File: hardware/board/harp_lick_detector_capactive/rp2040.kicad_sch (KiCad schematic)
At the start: 46 parts

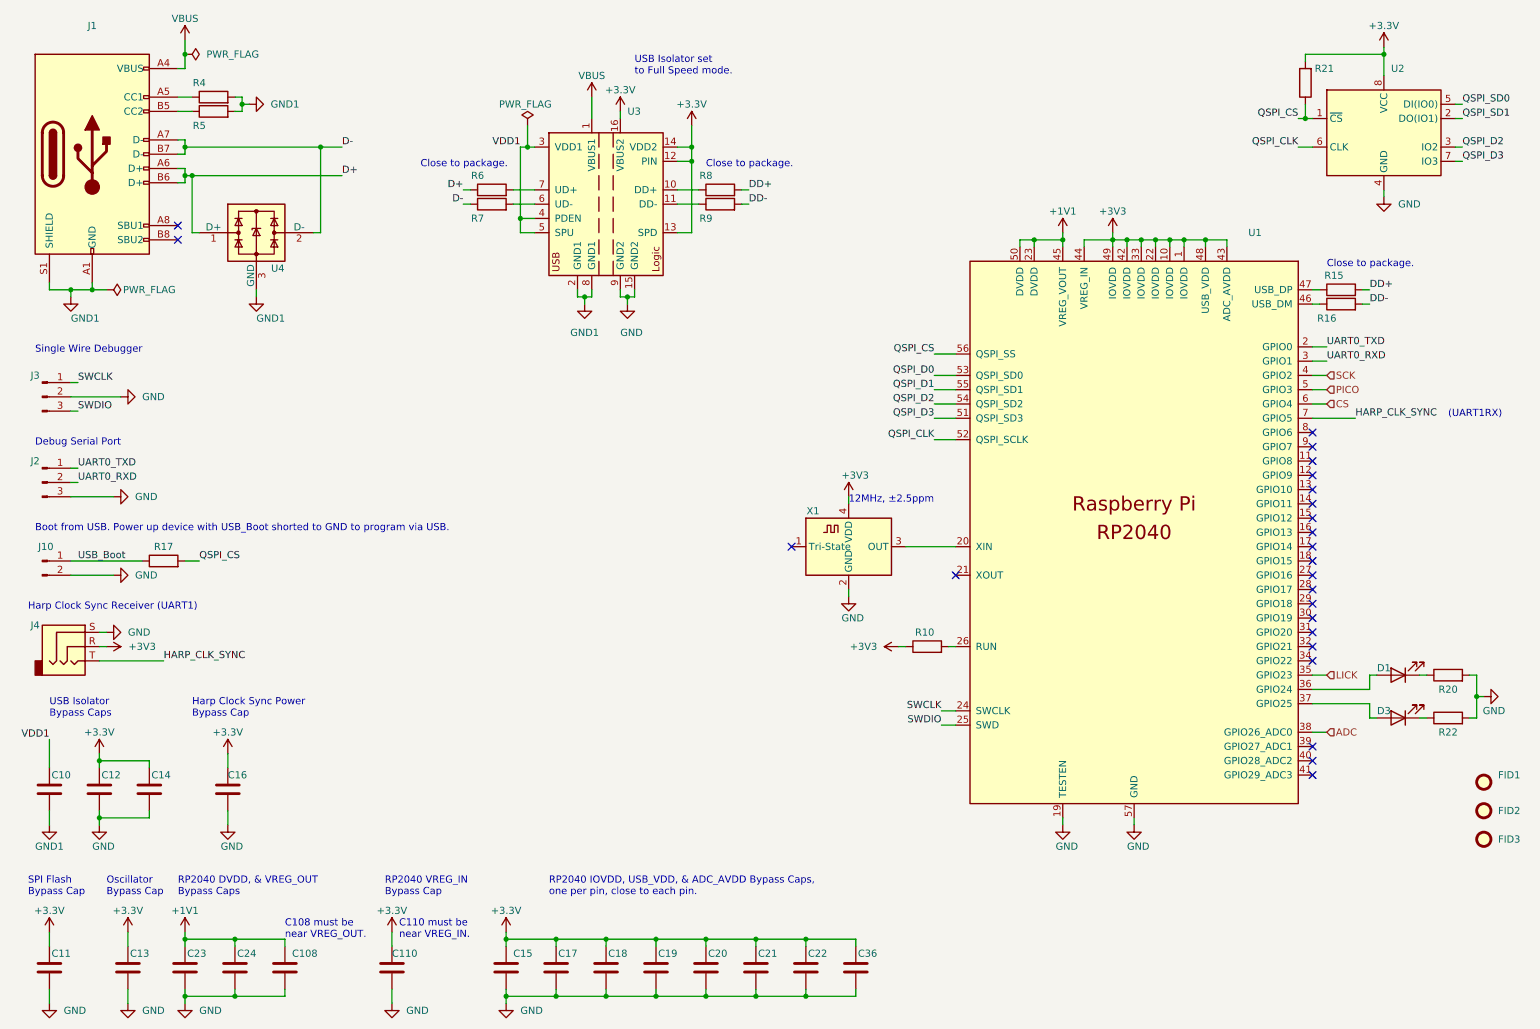
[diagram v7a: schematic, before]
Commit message: change usb connector; more layout
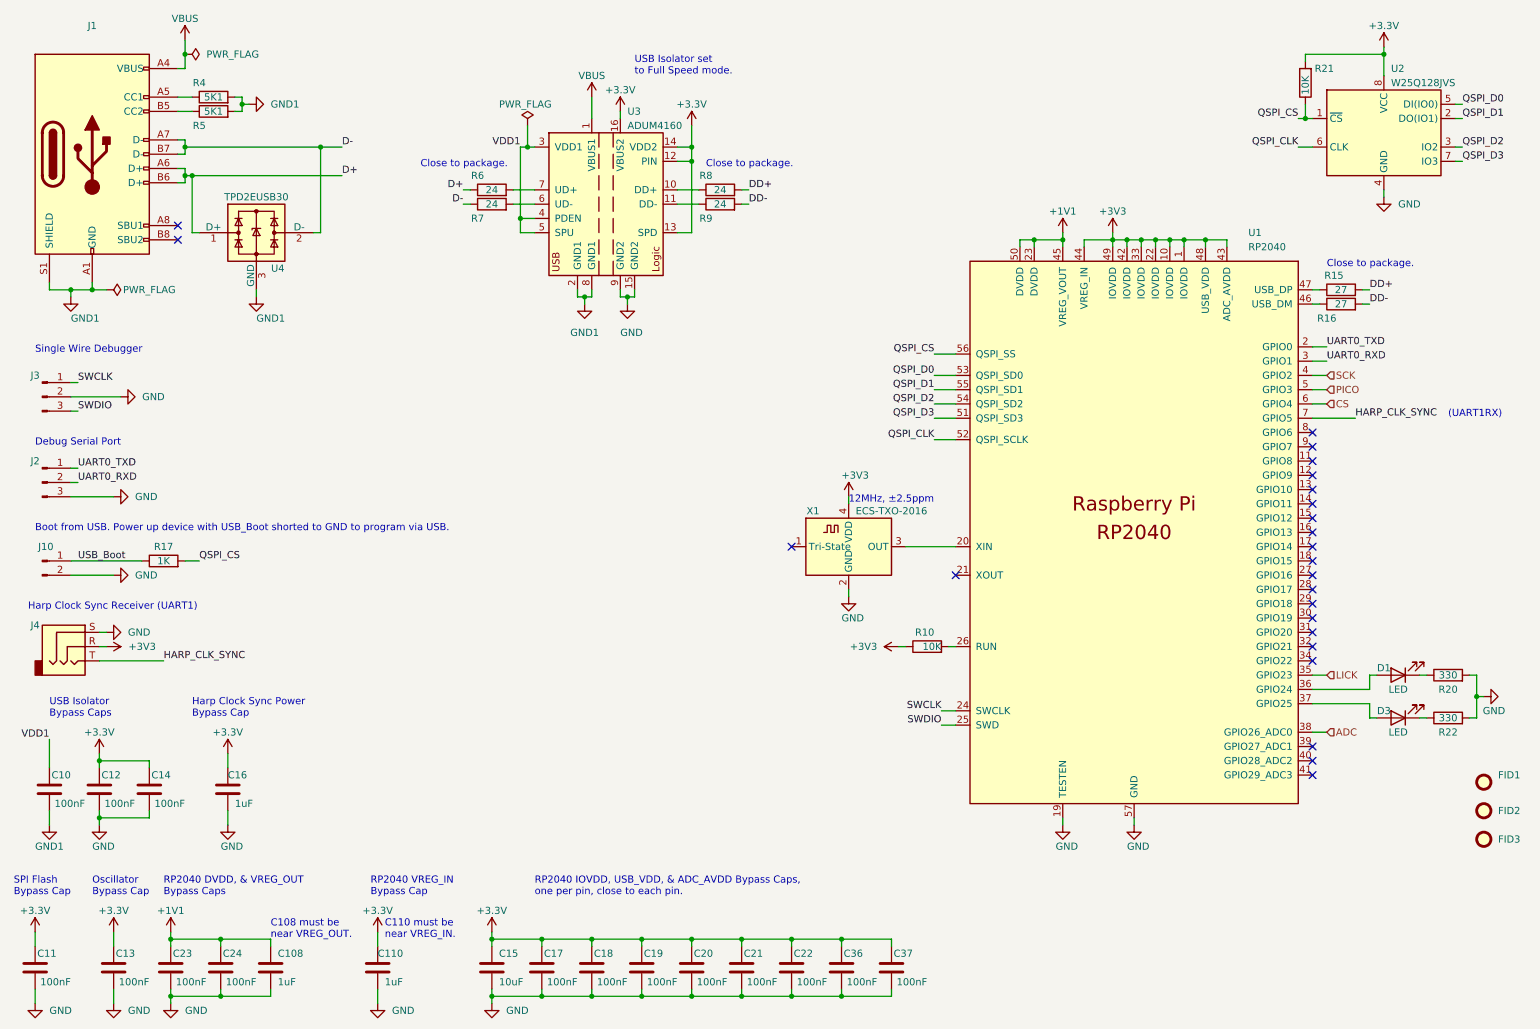
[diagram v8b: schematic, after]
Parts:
- added C37: 100nF, Capacitor_SMD:C_0402_1005Metric_Pad0.74x0.62mm_HandSolder, symbol Device:C
- C10, C11, C12, C13, C14, C17, C18, C19, C20, C21, C22, C23, C24, C36: value (none) -> 100nF; footprint (none) -> Capacitor_SMD:C_0402_1005Metric_Pad0.74x0.62mm_HandSolder
- C108, C110, C16: value (none) -> 1uF; footprint (none) -> Capacitor_SMD:C_0603_1608Metric_Pad1.08x0.95mm_HandSolder
- C15: value (none) -> 10uF; footprint (none) -> Capacitor_SMD:C_0805_2012Metric
- D1, D3: value (none) -> LED; footprint (none) -> LED_SMD:LED_0603_1608Metric_Pad1.05x0.95mm_HandSolder
- FID1, FID2, FID3: value (none) -> Fiducial; footprint (none) -> Fiducial:Fiducial_0.5mm_Mask1mm
- J1: Link https://www.digikey.com/en/products/detail/amphenol-cs-comm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 -> https://www.digikey.com/en/products/detail/jae-electronics/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; Manufacturer Amphenol ICC (Commercial Products) -> JAE Electronics; Manufacturer Number 12401610E4#2A -> DX07S016JA1R1500
- J10: value (none) -> Conn_01x02_Male; footprint (none) -> Connector_PinHeader_2.54mm:PinHeader_1x02_P2.54mm_Vertical
- J2, J3: value (none) -> Conn_01x03_Male; footprint (none) -> Connector_PinHeader_2.54mm:PinHeader_1x03_P2.54mm_Vertical
- J4: value (none) -> AudioJack3; footprint (none) -> Connector_Audio:Jack_3.5mm_CUI_SJ-3523-SMT_Horizontal
- R10, R21: value (none) -> 10K; footprint (none) -> Resistor_SMD:R_0402_1005Metric_Pad0.72x0.64mm_HandSolder
- R15, R16: value (none) -> 27; footprint (none) -> Resistor_SMD:R_0402_1005Metric_Pad0.72x0.64mm_HandSolder
- R17: value (none) -> 1K; footprint (none) -> Resistor_SMD:R_0402_1005Metric_Pad0.72x0.64mm_HandSolder
- R20, R22: value (none) -> 330; footprint (none) -> Resistor_SMD:R_0603_1608Metric_Pad0.98x0.95mm_HandSolder
- R4, R5: value (none) -> 5K1; footprint (none) -> Resistor_SMD:R_0603_1608Metric_Pad0.98x0.95mm_HandSolder
- R6, R7, R8, R9: value (none) -> 24; footprint (none) -> Resistor_SMD:R_0402_1005Metric_Pad0.72x0.64mm_HandSolder
- U1: value (none) -> RP2040; footprint (none) -> machine_agency_components:RP2040-QFN-56
- U2: value (none) -> W25Q128JVS; footprint (none) -> Package_SO:SOIC-8_5.23x5.23mm_P1.27mm
- U3: value (none) -> ADUM4160; footprint (none) -> Package_SO:SOIC-16W_7.5x10.3mm_P1.27mm
- U4: value (none) -> TPD2EUSB30; footprint (none) -> Package_TO_SOT_SMD:Texas_DRT-3
- X1: value (none) -> ECS-TXO-2016; footprint (none) -> Crystal:Crystal_SMD_2016-4Pin_2.0x1.6mm
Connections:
- net QSPI_SD0 is gone; now on net QSPI_D0: U2.5 (DI(IO0))
- net QSPI_SD1 is gone; now on net QSPI_D1: U2.2 (DO(IO1))
- net +3V3: now also C37.2
- net GND: now also C37.1
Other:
- moved on the sheet: C108, C11, C110, C13, C15, C17, C18, C19, C20, C21, C22, C23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
